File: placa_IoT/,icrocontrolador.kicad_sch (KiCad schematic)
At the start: 0 parts

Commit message: Microprocesador in progress izq
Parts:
- added C10, C5: 10 uF, Capacitor_SMD:C_0402_1005Metric, symbol Device:C
- added C11, C6: 1 uF, Capacitor_SMD:C_0402_1005Metric, symbol Device:C
- added C12, C13, C20, C7: 100 nF, Capacitor_SMD:C_0402_1005Metric, symbol Device:C
- added C14, C15, C16, C17, C18, C19: NC, Capacitor_SMD:C_0402_1005Metric, symbol Device:C
- added C8, C9: 12 pF, Capacitor_SMD:C_0402_1005Metric, symbol Device:C
- added L2: 2 nH, Inductor_SMD:L_0402_1005Metric, symbol Device:L
- added L3: 22 nH, Inductor_SMD:L_0402_1005Metric, symbol Device:L
- added R4, R5: NC, Resistor_SMD:R_0402_1005Metric, symbol Device:R
- added U3: ESP32-S3, ic_control:QFN-56-1EP_7x7mm_P0.4mm_EP4x4mm, symbol ic_control:ESP32-S3
- added U4: PRO-OB-536, antennas:ANTENNA_PIFA_3D_2.4GHZ, symbol antennas:ANTENNA_PIFA_3D_2.4GHZ
- added Y1: 40 MHz, Crystal:Crystal_SMD_3225-4Pin_3.2x2.5mm, symbol Device:Crystal_GND24
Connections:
- new net: C18.1, C19.2, U4.2 (FEED)
- new net: C15.2, C16.1, C17.2, C18.2
- new net: C14.2, C16.2, U3.1 (LNA_IN)
- new net: C13.1, L2.2, U3.2 (VDD3P3), U3.3 (VDD3P3)
- new net: R5.1, U3.49 (U0TXD)
- new net: C9.1, U3.53 (XTAL_N), Y1.3
- new net: L3.2, U3.54 (XTAL_P)
- new net: C8.1, L3.1, Y1.1
- new net: Y1.2 (G), Y1.4 (G)
- new net +3.3V: C10.1, C11.1, C12.1, C20.1, C5.1, C6.1, C7.1, L2.1, R4.1, U3.20 (VDD3P3_RTC), U3.46 (VDD3P3_CPU), U3.55 (VDDA), U3.56 (VDDA)
- new net CDM-M0S1-IO11: U3.16 (GPIO11)
- new net CLK-SCK-IO14: U3.19 (GPIO14)
- new net GND: C10.2, C11.2, C12.2, C13.2, C14.1, C15.1, C17.1, C19.1, C20.2, C5.2, C6.2, C7.2, C8.2, C9.2, U3.57 (GND), U4.1 (GND)
- new net IO0: U3.5 (GPIO0)
- new net IO1: U3.6 (GPIO1)
- new net IO12: U3.17 (GPIO12)
- new net IO17: U3.23 (GPIO17)
- new net IO18: U3.24 (GPIO18)
- new net IO19: U3.25 (GPIO19/USB_D-)
- new net IO20: U3.26 (GPIO20/USB_D+)
- new net IO3: U3.8 (GPIO3)
- new net IO4: U3.9 (GPIO4)
- new net IO45: R4.2, U3.51 (GPIO45)
- new net IO5: U3.10 (GPIO5)
- new net IO6: U3.11 (GPIO6)
- new net IO7: U3.12 (GPIO7)
- new net IO8: U3.13 (GPIO8)
- new net IO9: U3.14 (GPIO9)
- new net LORA_RX: U3.27 (GPIO21)
- new net LORA_TX: U3.15 (GPIO10)
- new net RST/EN: U3.4 (CHIP_PU)
- new net SD3-CS-IO13: U3.18 (GPIO13)
- new net SDO-MISO-IO2: U3.7 (GPIO2)
- new net UGTXD: R5.2
- no-connect marks 0 -> 8

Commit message: Microprocesador dcha add
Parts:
- R5: value NC -> 499 Ohm
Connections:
- net IO15: now reaches U3.21 (XTAL_32K_P)
- net IO16: now reaches U3.22 (XTAL_32K_N)
- net IO48: now reaches U3.36 (SPICLK_N)
- net IO47: now reaches U3.37 (SPICLK_P)
- net IO33: now reaches U3.38 (GPIO33)
- net IO34: now reaches U3.39 (GPIO34)
- net IO35: now reaches U3.40 (GPIO35)
- net IO36: now reaches U3.41 (GPIO36)
- net IO37: now reaches U3.42 (GPIO37)
- net IO38: now reaches U3.43 (GPIO38)
- net IO39/MTCK: now reaches U3.44 (MTCK)
- net IO40/MTDO: now reaches U3.45 (MTDO)
- net IO41/MTDI: now reaches U3.47 (MTDI)
- net IO42/MTMS: now reaches U3.48 (MTMS)
- net UORXD: now reaches U3.50 (U0RXD)
- net IO46: now reaches U3.52 (GPIO46)
- net UGTXD renamed UOTXD

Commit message: Microprocesador total
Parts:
- added C21: 1 uF, Capacitor_SMD:C_0402_1005Metric, symbol Device:C
- added J1, J2: 22-28-4144, connectors:CONN_THT_MV_PH_P2.54MM_P14, symbol connectors:CONN_THT_MV_PH_P2.54MM_P14
- added R6, R7: 10 kOhm, Resistor_SMD:R_0402_1005Metric, symbol Device:R
- added SW1: RST/EN, Button_Switch_SMD:SW_Push_SPST_NO_Alps_SKRK, symbol Switch:SW_Push
- added SW2: BODT, Button_Switch_SMD:SW_Push_SPST_NO_Alps_SKRK, symbol Switch:SW_Push
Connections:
- net RST/EN is gone; now on net GND: U3.4 (CHIP_PU)
- net +3.3V: now also J1.3 (Pin_3), R6.2, R7.2
- net GND: now also C21.1, C21.2, J1.2 (Pin_2), J1.4 (Pin_4), J2.11 (Pin_11), J2.14 (Pin_14), R6.1, SW1.1, SW1.2, SW2.1
- net IO0: now also J2.3 (Pin_3)
- net IO12: now also J2.10 (Pin_10)
- net IO15: now also J2.12 (Pin_12)
- net IO16: now also J2.13 (Pin_13)
- net IO33: now also J2.6 (Pin_6)
- net IO34: now also J2.5 (Pin_5)
- net IO35: now also J2.4 (Pin_4)
- net IO36: now also J2.2 (Pin_2)
- net IO37: now also J2.1 (Pin_1)
- net IO38: now also J1.13 (Pin_13)
- net IO39/MTCK: now also J1.10 (Pin_10)
- net IO40/MTDO: now also J1.9 (Pin_9)
- net IO41/MTDI: now also J1.8 (Pin_8)
- net IO42/MTMS: now also J1.5 (Pin_5)
- net IO45: now also J1.7 (Pin_7)
- net IO46: now also J1.6 (Pin_6)
- net IO47: now also J2.7 (Pin_7)
- net IO48: now also J2.8 (Pin_8)
- net IO8: now also J2.9 (Pin_9)
- net UORXD: now also J1.11 (Pin_11)
- net UOTXD: now also J1.12 (Pin_12)
- net at C15.2, C16.1, C18.2: no longer C17.2
- new net IDO: R7.1, SW2.2
- new net VBAT: J1.14 (Pin_14)
- new net VBUS: J1.1 (Pin_1)
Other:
- moved on the sheet: C18, C19, C8, C9, L3, U4, Y1

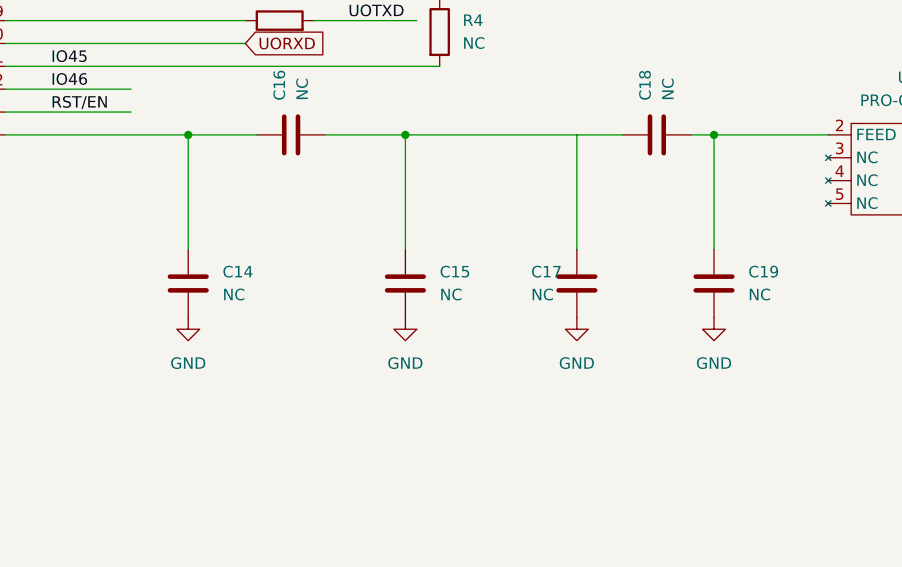
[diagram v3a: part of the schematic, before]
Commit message: No conectar elementos
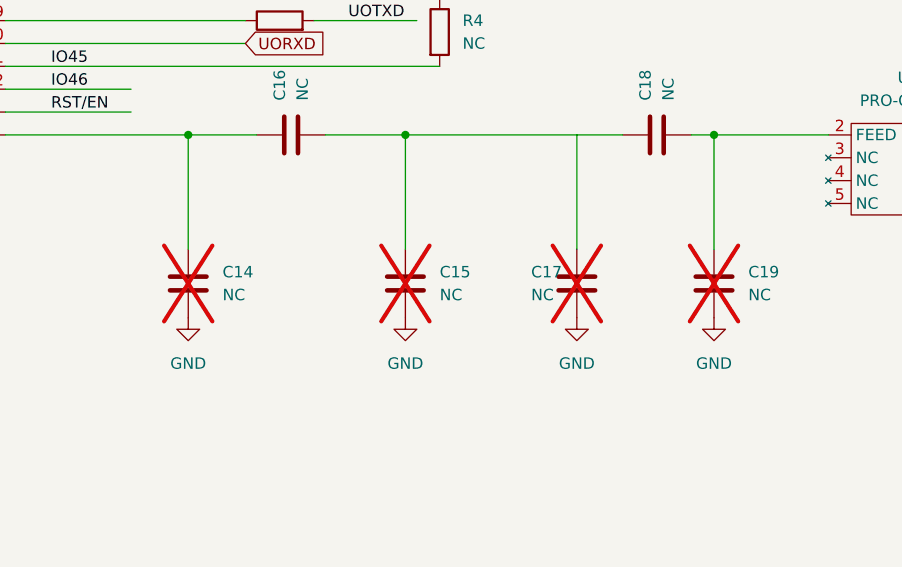
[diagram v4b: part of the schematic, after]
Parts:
- C14, C15, C17, C19: now not fitted
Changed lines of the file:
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@@
 		(on_board yes)
 		(in_pos_files yes)
-		(dnp no)
+		(dnp yes)
 		(fields_autoplaced yes)
 		(property "Reference" "C15"
@@
 		(on_board yes)
 		(in_pos_files yes)
-		(dnp no)
+		(dnp yes)
 		(fields_autoplaced yes)
 		(property "Reference" "C19"
@@
 		(on_board yes)
 		(in_pos_files yes)
-		(dnp no)
+		(dnp yes)
 		(fields_autoplaced yes)
 		(property "Reference" "C14"
@@
 		(on_board yes)
 		(in_pos_files yes)
-		(dnp no)
+		(dnp yes)
 		(property "Reference" "C17"
 			(at 203.2 146.0499 0)

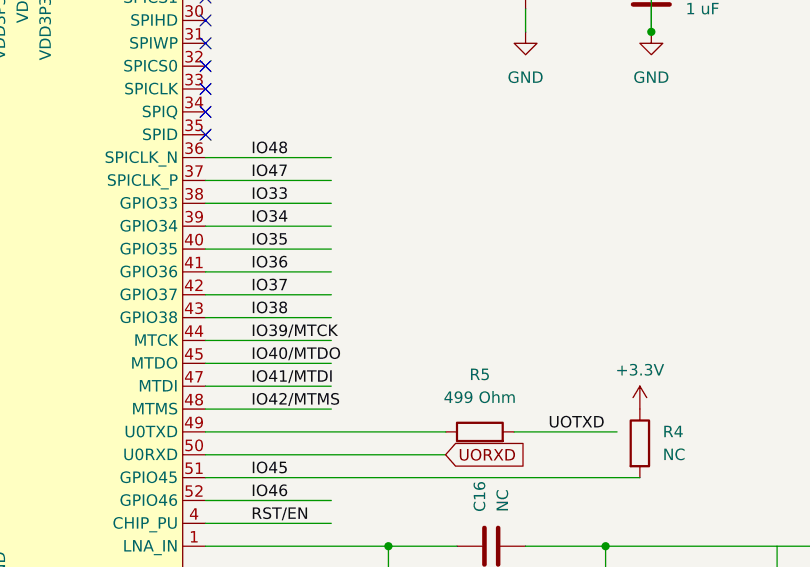
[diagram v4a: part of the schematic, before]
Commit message: Diodo led micro IO37 add
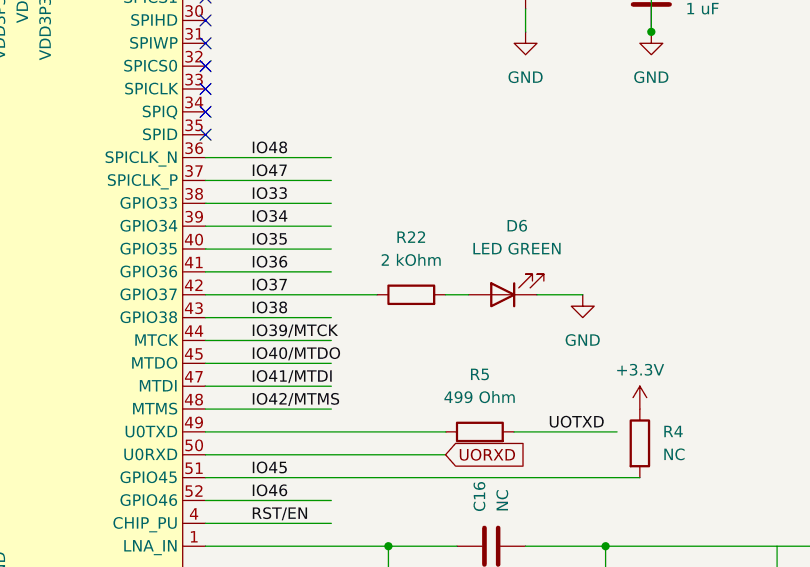
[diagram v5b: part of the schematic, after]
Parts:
- added D6: LED GREEN, LED_SMD:LED_0402_1005Metric, symbol Device:LED
- added R22: 2 kOhm, Resistor_SMD:R_0402_1005Metric, symbol Device:R
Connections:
- net GND: now also D6.1 (K)
- net IO37: now also R22.1
- new net: D6.2 (A), R22.2

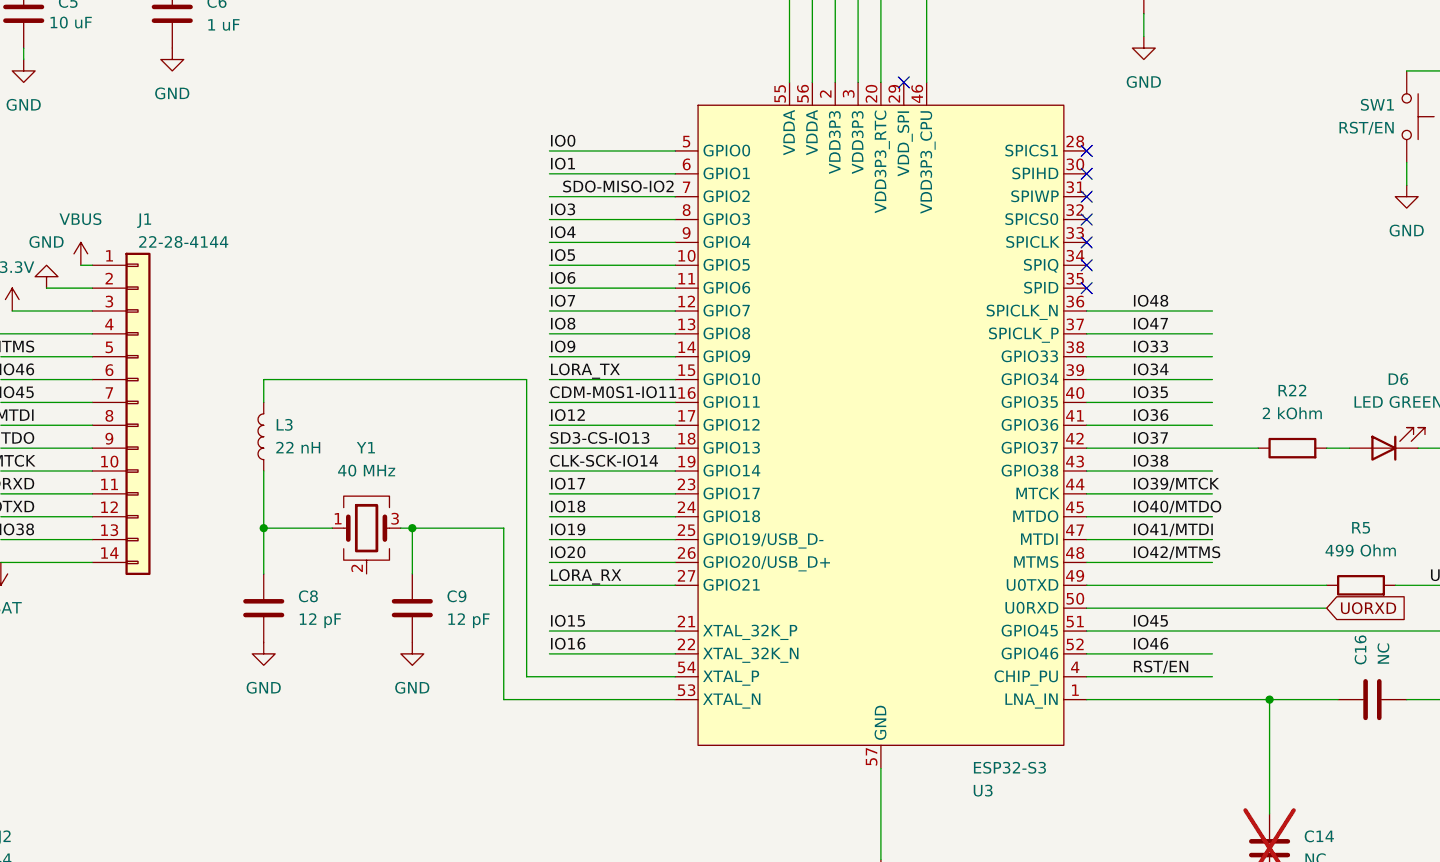
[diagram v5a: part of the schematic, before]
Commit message: Falta unir pines
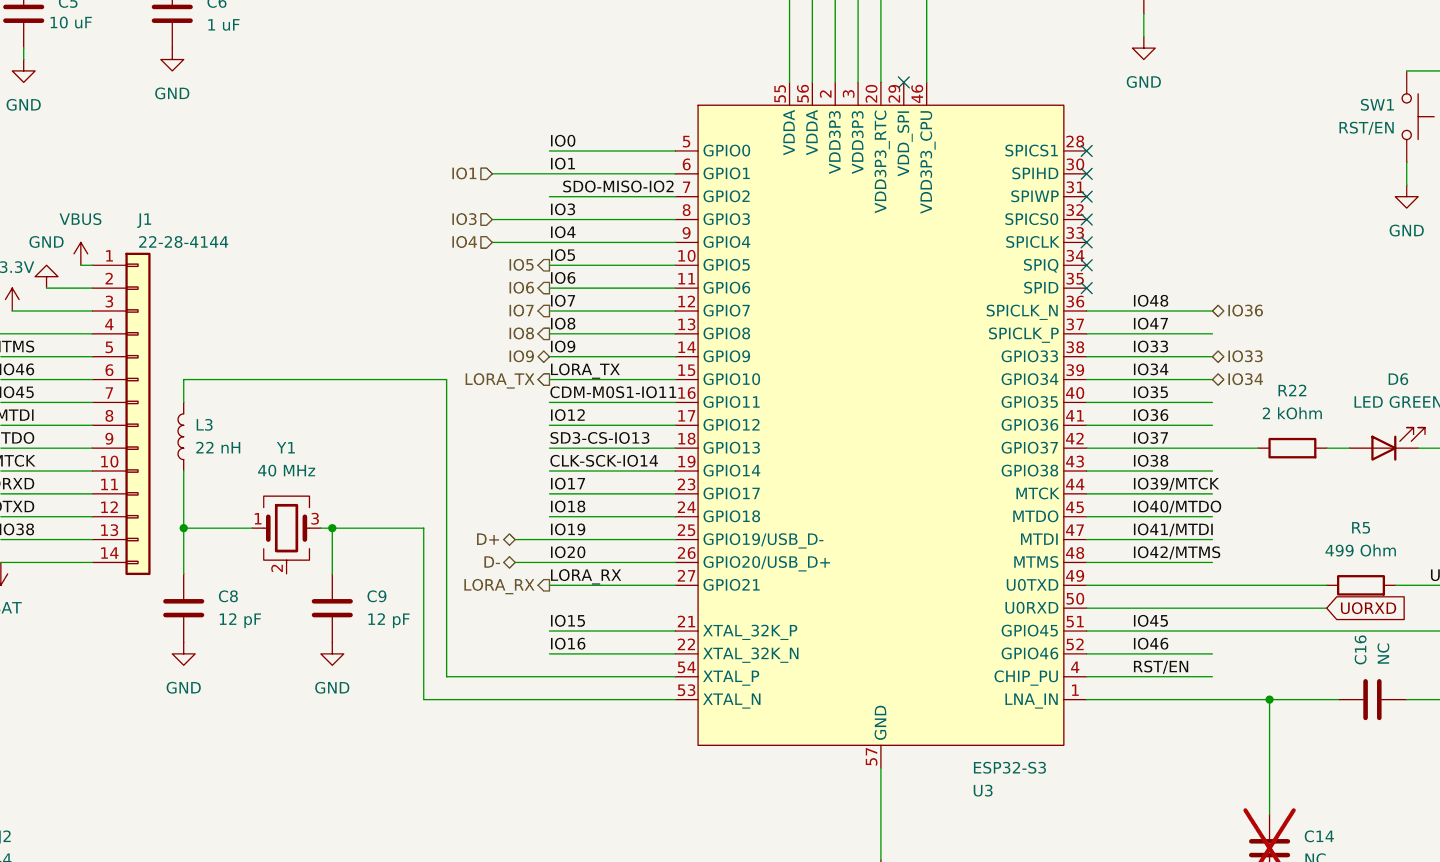
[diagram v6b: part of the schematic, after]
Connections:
- net IO48 is gone; now on net IO36: J2.8 (Pin_8), U3.36 (SPICLK_N)
- net IO19 renamed D+
- net IO20 renamed D-
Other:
- moved on the sheet: C8, C9, L3, Y1
